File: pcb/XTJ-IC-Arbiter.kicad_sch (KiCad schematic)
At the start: 50 parts, among them J1 TSW-101-07-T-D, J2 TSW-101-07-T-D, J3 DTM13-12PA-R008, U1 LM2672N-5.0, U2 CDP68HC68S1, U3 Teensy4.0, U4 MCP2562-H-P, U5 MCP1700-1802E_TO92

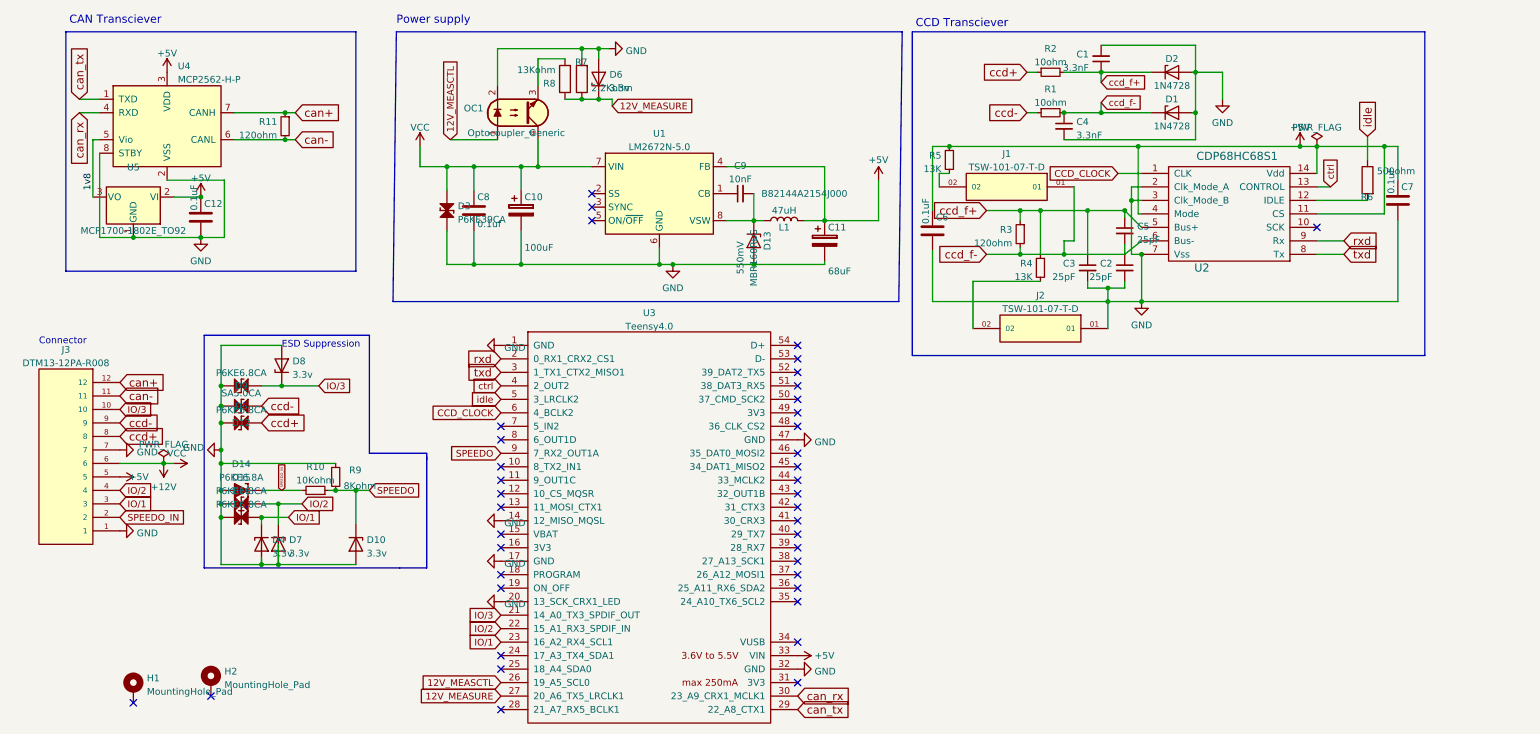
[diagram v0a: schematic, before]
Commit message: After breadboarding, eliminate LDO reference regulator
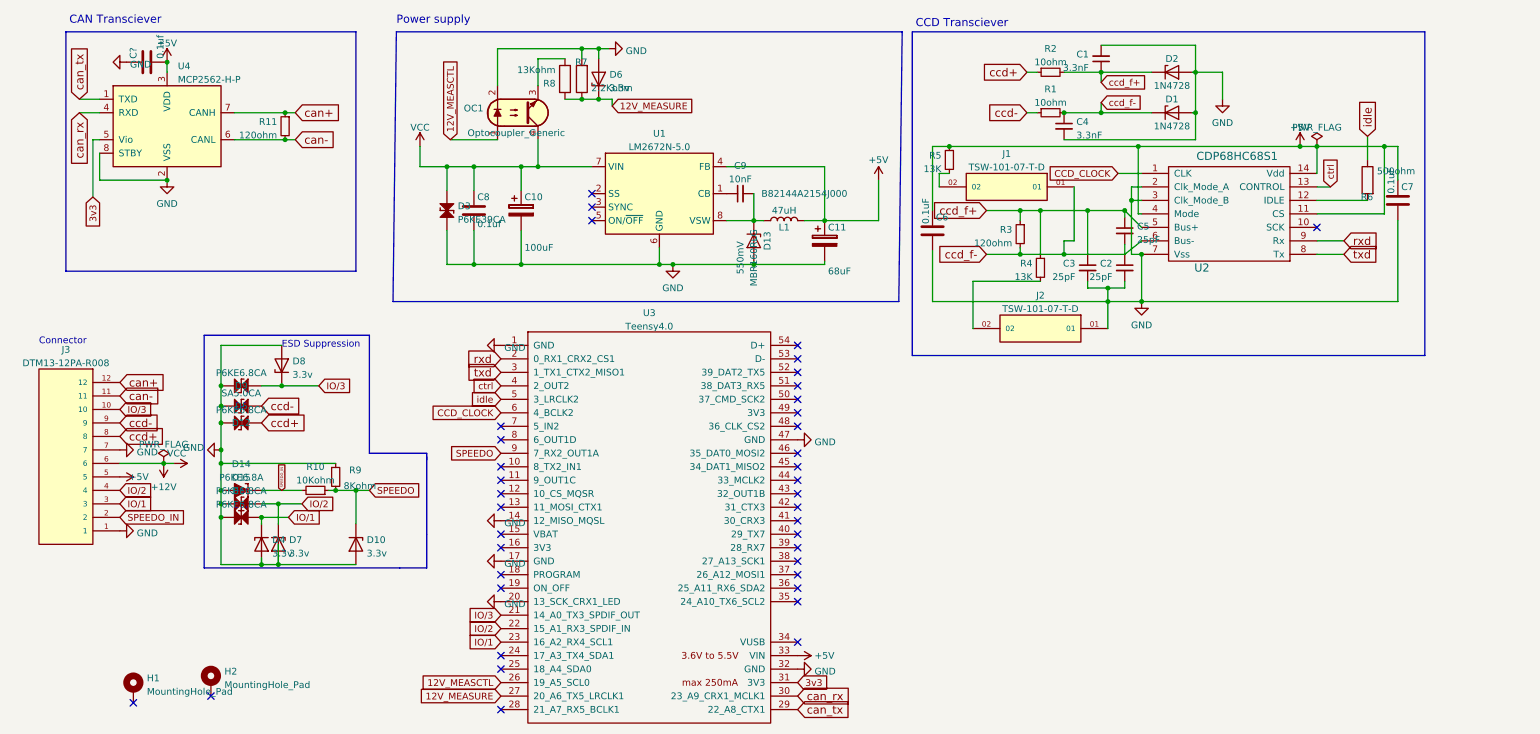
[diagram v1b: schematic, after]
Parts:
- removed C12: 0.1uF, Capacitor_THT:C_Disc_D3.8mm_W2.6mm_P2.50mm, symbol ccd_can_bridge-rescue:C
- removed U5: MCP1700-1802E_TO92, Package_TO_SOT_THT:TO-92_Inline, symbol Regulator_Linear:MCP1700-1802E_TO92
- added C?: 0.1uf, Capacitor_THT:C_Disc_D3.8mm_W2.6mm_P2.50mm, symbol ccd_can_bridge-rescue:C
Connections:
- net 1v8 is gone; now on net 3v3: U4.5 (Vio)
- net +5V: now also C?.2
- net GND: now also C?.1
- net 3v3: now reaches U3.31 (3V3)
- no-connect marks 40 -> 39

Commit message: More tweaking
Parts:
- added C13: 0.1uf, Capacitor_THT:C_Disc_D3.8mm_W2.6mm_P2.50mm, symbol ccd_can_bridge-rescue:C
- gave numbers to parts that had none: 1
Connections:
- net 3v3: now also C13.1
- net GND: now also C13.2
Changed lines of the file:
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@@
   (junction (at 52.705 107.315) (diameter 0) (color 0 0 0 0)
   )
+  (junction (at 36.195 46.355) (diameter 0) (color 0 0 0 0)
+  )
   (junction (at 153.035 62.23) (diameter 0) (color 0 0 0 0)
   )
@@
   )
   (junction (at 189.865 40.005) (diameter 0) (color 0 0 0 0)
+  )
+  (junction (at 28.575 48.895) (diameter 0) (color 0 0 0 0)
   )
   (junction (at 211.455 33.655) (diameter 0) (color 0 0 0 0)
@@
     (stroke (width 0) (type default) (color 0 0 0 0))
   )
-  (wire (pts (xy 28.575 38.735) (xy 28.575 49.53))
+  (wire (pts (xy 28.575 38.735) (xy 28.575 48.895))
     (stroke (width 0) (type default) (color 0 0 0 0))
   )
@@
     (stroke (width 0) (type default) (color 0 0 0 0))
   )
+  (wire (pts (xy 28.575 48.895) (xy 28.575 49.53))
+    (stroke (width 0) (type default) (color 0 0 0 0))
+  )
   (wire (pts (xy 219.71 66.675) (xy 219.71 69.215))
     (stroke (width 0) (type default) (color 0 0 0 0))
@@
     (stroke (width 0) (type default) (color 0 0 0 0))
   )
-  (wire (pts (xy 29.845 46.355) (xy 42.545 46.355))
+  (wire (pts (xy 29.845 46.355) (xy 36.195 46.355))
     (stroke (width 0) (type default) (color 0 0 0 0))
   )
@@
     (stroke (width 0) (type default) (color 0 0 0 0))
   )
+  (wire (pts (xy 36.195 46.355) (xy 36.195 48.895))
+    (stroke (width 0) (type default) (color 0 0 0 0))
+  )
   (wire (pts (xy 147.955 53.975) (xy 153.035 53.975))
     (stroke (width 0) (type default) (color 0 0 0 0))
@@
   )
   (wire (pts (xy 203.2 52.07) (xy 207.01 52.07))
+    (stroke (width 0) (type default) (color 0 0 0 0))
+  )
+  (wire (pts (xy 36.195 46.355) (xy 42.545 46.355))
     (stroke (width 0) (type default) (color 0 0 0 0))
   )
@@
   (symbol (lib_id "power:GND") (at 34.925 24.13 270) (unit 1)
     (in_bom yes) (on_board yes) (fields_autoplaced)
-    (property "Reference" "#PWR?" (id 0) (at 28.575 24.13 0)
+    (property "Reference" "#PWR0108" (id 0) (at 28.575 24.13 0)
       (effects (font (size 1.27 1.27)) hide)
     )
@@
     (pin "2")
   )
+  (symbol (lib_id "ccd_can_bridge-rescue:C") (at 32.385 48.895 90) (unit 1)
+    (in_bom yes) (on_board yes)
+    (property "Reference" "C13" (id 0) (at 29.845 48.26 0)
+      (effects (font (size 1.27 1.27)) (justify left))
+    )
+    (property "Value" "0.1uf" (id 1) (at 34.925 48.26 0)
+      (effects (font (size 1.27 1.27)) (justify left))
+    )
+    (property "Footprint" "Capacitor_THT:C_Disc_D3.8mm_W2.6mm_P2.50mm" (id 2) (at 36.195 47.9298 0)
+      (effects (font (size 1.27 1.27)) hide)
+    )
+    (property "Datasheet" "" (id 3) (at 32.385 48.895 0))
+    (pin "1")
+    (pin "2")
+  )
   (symbol (lib_id "Device:R_Small") (at 208.915 26.035 90) (mirror x) (unit 1)
     (in_bom yes) (on_board yes) (fields_autoplaced)
@@
   (symbol (lib_id "ccd_can_bridge-rescue:C") (at 38.735 24.13 90) (unit 1)
     (in_bom yes) (on_board yes)
-    (property "Reference" "C?" (id 0) (at 36.195 23.495 0)
+    (property "Reference" "C12" (id 0) (at 36.195 23.495 0)
       (effects (font (size 1.27 1.27)) (justify left))
     )
@@
     )
     (path "/0ea7c072-d6e1-405c-a884-f01b163ec300"
-      (reference "#PWR?") (unit 1) (value "GND") (footprint "")
+      (reference "#PWR0108") (unit 1) (value "GND") (footprint "")
     )
     (path "/f47f0eb3-3cf7-4f49-944e-082f208869f2"
@@
     )
     (path "/cac6c477-5b9f-4115-a36a-335bf8924592"
-      (reference "C?") (unit 1) (value "0.1uf") (footprint "Capacitor_THT:C_Disc_D3.8mm_W2.6mm_P2.50mm")
+      (reference "C12") (unit 1) (value "0.1uf") (footprint "Capacitor_THT:C_Disc_D3.8mm_W2.6mm_P2.50mm")
+    )
+    (path "/200bea53-c26b-4680-9c37-95b9c615c9f3"
+      (reference "C13") (unit 1) (value "0.1uf") (footprint "Capacitor_THT:C_Disc_D3.8mm_W2.6mm_P2.50mm")
     )
     (path "/1b315b47-8adf-49de-916b-225f0c5df700"

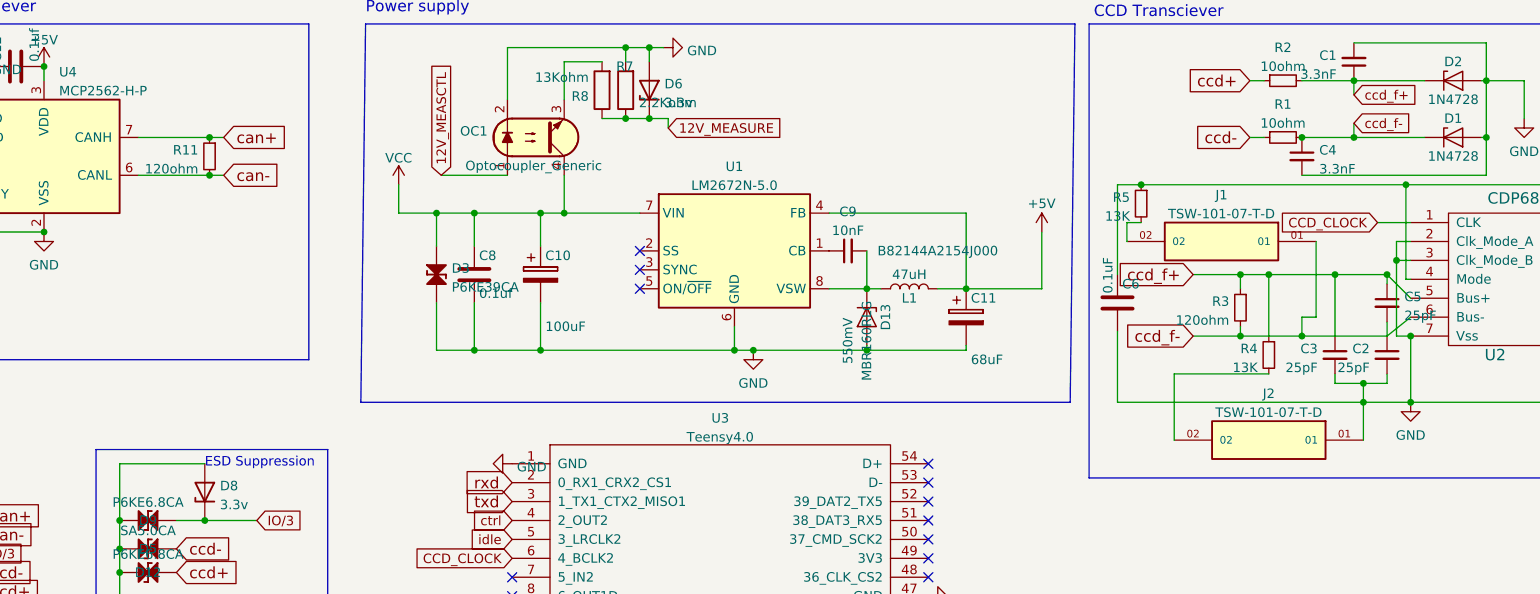
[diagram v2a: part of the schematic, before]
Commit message: Switch from jumpers to DIP switches for CCD bias, CCD bus termination.  Add DIP switch for selectable CAN bus termination.  DIP switches should hold up in vibration, where I worry a jumper might rattle off
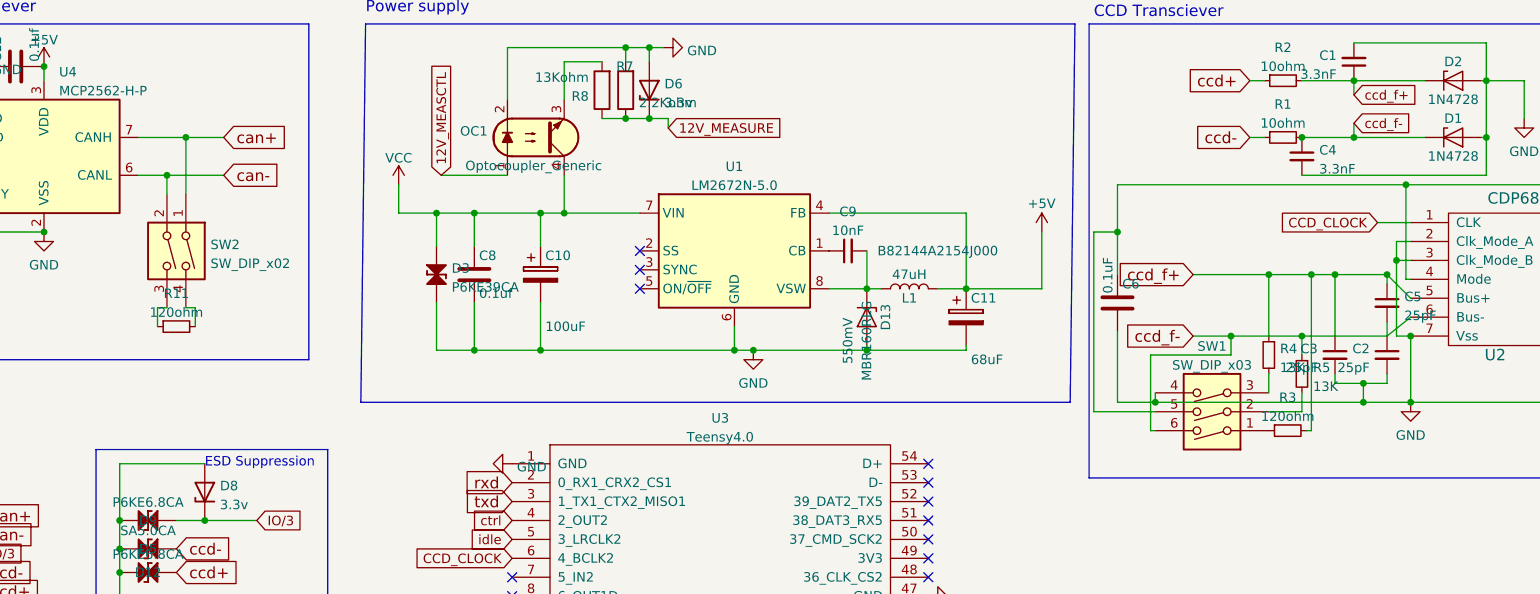
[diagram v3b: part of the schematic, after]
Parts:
- removed J1, J2: TSW-101-07-T-D, Jumpers:SAMTEC_TSW-101-07-T-D, symbol TSW-101-07-T-D:TSW-101-07-T-D
- added SW1: SW_DIP_x03, Button_Switch_THT:SW_DIP_SPSTx03_Slide_9.78x9.8mm_W7.62mm_P2.54mm, symbol Switch:SW_DIP_x03
- added SW2: SW_DIP_x02, Button_Switch_THT:SW_DIP_SPSTx02_Slide_9.78x7.26mm_W7.62mm_P2.54mm, symbol Switch:SW_DIP_x02
- R5: footprint Resistor_THT:R_Axial_DIN0207_L6.3mm_D2.5mm_P7.62mm_Horizontal -> Resistor_THT:R_Axial_DIN0207_L6.3mm_D2.5mm_P2.54mm_Vertical
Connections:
- net +5V: now also SW1.5; no longer R5.1
- net GND: now also SW1.4
- net can+: now also SW2.1; no longer R11.1
- net can-: now also SW2.2; no longer R11.2
- net ccd_f+: now also R3.2; no longer R3.1
- net ccd_f-: now also R5.1, SW1.6; no longer R3.2
- net at R5.2: now also SW1.2
- net at R4.2: now also SW1.3
- new net: R11.1, SW2.3
- new net: R11.2, SW2.4
- new net: R3.1, SW1.1
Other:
- moved on the sheet: R11, R3, R5

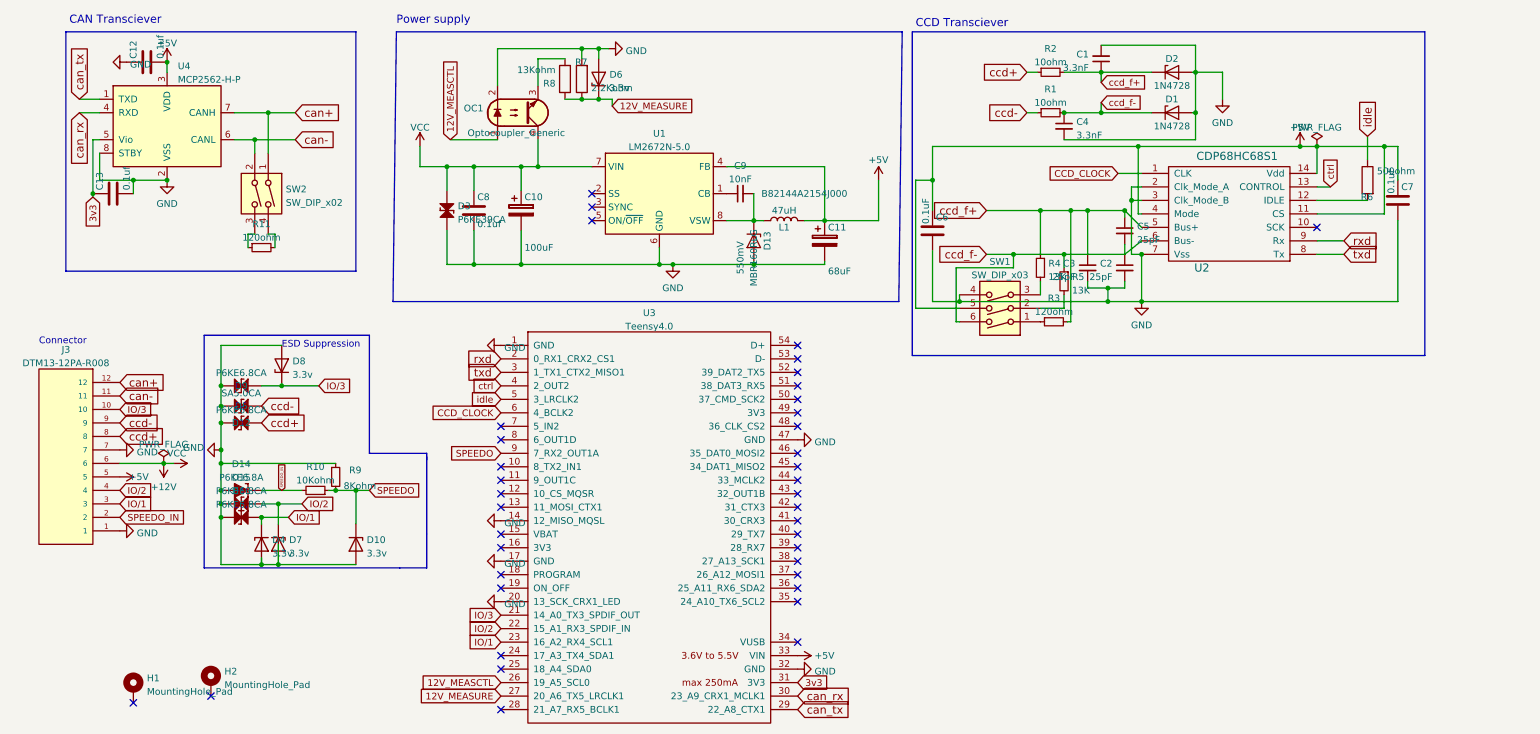
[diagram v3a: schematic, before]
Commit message: Add a level shifter to handle 5v to 3.3v for the CDP<->Teensy
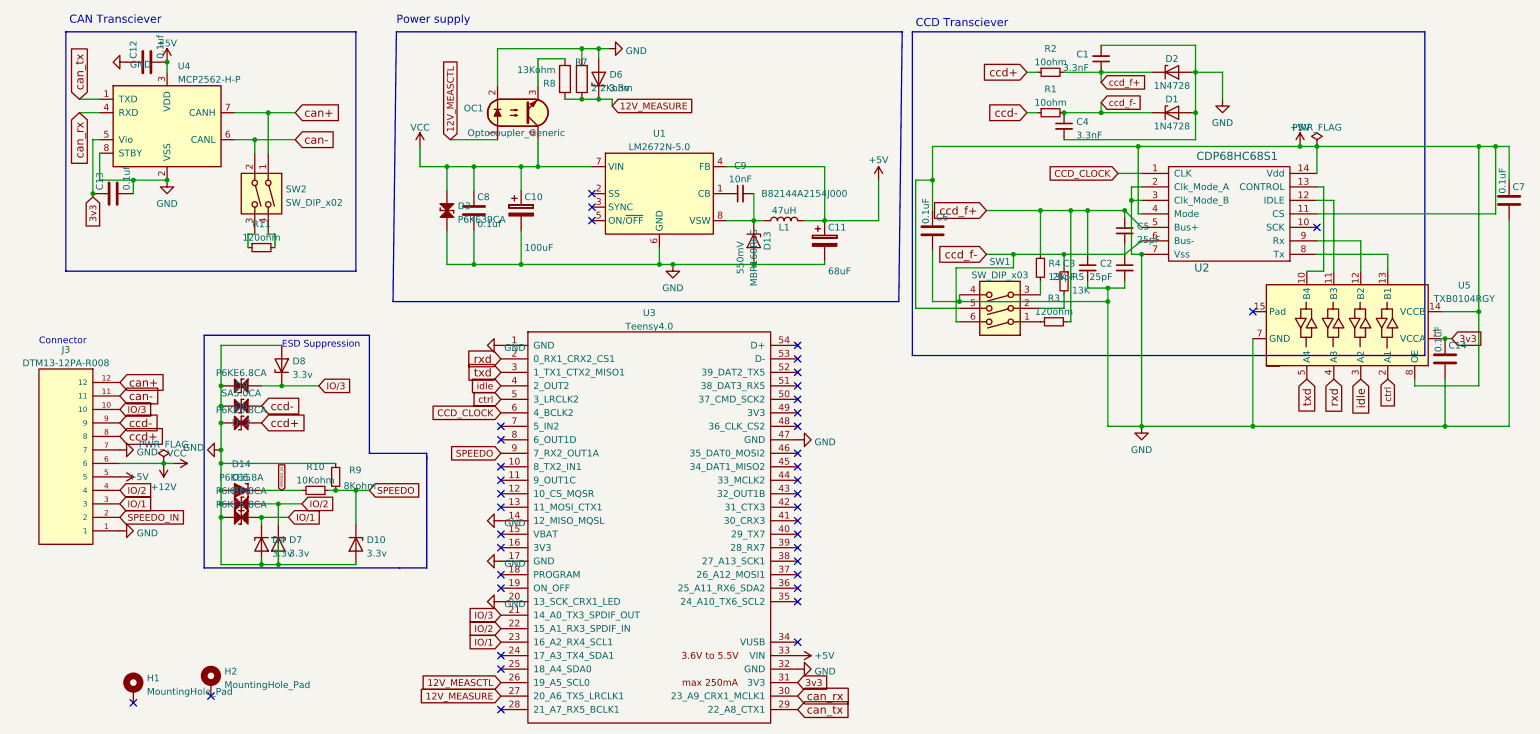
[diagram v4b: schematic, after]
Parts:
- removed R6: 500ohm, Resistor_THT:R_Axial_DIN0204_L3.6mm_D1.6mm_P5.08mm_Horizontal, symbol Device:R
- added C14: 0.1uF, Capacitor_THT:C_Disc_D3.8mm_W2.6mm_P2.50mm, symbol ccd_can_bridge-rescue:C
- added U5: TXB0104RGY, Package_SO:SOIC-14_3.9x8.7mm_P1.27mm, symbol Logic_LevelTranslator:TXB0104RGY
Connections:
- net +5V: now also U5.14 (VCCB), U5.8 (OE)
- net 3v3: now also C14.1, U5.1 (VCCA)
- net GND: now also C14.2, U5.7 (GND)
- net ctrl: now also U3.5 (3_LRCLK2), U5.2 (A1); no longer U2.13 (CONTROL), U3.4 (2_OUT2)
- net idle: now also U3.4 (2_OUT2), U5.3 (A2); no longer U3.5 (3_LRCLK2)
- net rxd: now also U5.4 (A3); no longer U2.9 (Rx)
- net txd: now also U5.5 (A4); no longer U2.8 (Tx)
- net at U2.12 (IDLE): now also U5.11 (B3)
- new net: U2.13 (CONTROL), U5.10 (B4)
- new net: U2.9 (Rx), U5.12 (B2)
- new net: U2.8 (Tx), U5.13 (B1)
- no-connect marks 39 -> 40
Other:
- moved on the sheet: C7
